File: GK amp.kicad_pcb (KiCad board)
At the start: 2 copper layers, 205.7 x 137.2 mm, 84 parts, among them J1 SPEAKER, J2 SPEAKER, J3 Direct Out, J4 AudioJack3, J5 IN, Q1 MPSA06, Q10 MJ-15002, Q11 TIP31, Q12 MPSA06, Q13 MPSA56*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

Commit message: Fix up footprints and layout PCB
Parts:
- C1, C3: footprint Capacitors_THT:C_Disc_D3.0mm_W1.6mm_P2.50mm -> Capacitor_THT:C_Rect_L9.0mm_W3.3mm_P7.50mm_MKT
- C10, C11: footprint Capacitors_THT:CP_Axial_L38.0mm_D18.0mm_P44.00mm_Horizontal -> Capacitor_THT:C_Rect_L9.0mm_W3.3mm_P7.50mm_MKT
- C12, C13, C14, C15: footprint Capacitors_THT:CP_Axial_L38.0mm_D18.0mm_P44.00mm_Horizontal -> Capacitor_THT:CP_Axial_L30.0mm_D18.0mm_P35.00mm_Horizontal
- C16, C17: footprint Capacitors_THT:CP_Axial_L38.0mm_D18.0mm_P44.00mm_Horizontal -> Capacitor_THT:CP_Axial_L10.0mm_D6.0mm_P15.00mm_Horizontal
- C18, C19: footprint Capacitors_THT:C_Disc_D3.0mm_W2.0mm_P2.50mm -> Capacitor_THT:C_Rect_L9.0mm_W3.3mm_P7.50mm_MKT
- C2: footprint Capacitors_THT:C_Axial_L3.8mm_D2.6mm_P7.50mm_Horizontal -> Capacitor_THT:CP_Radial_D8.0mm_P5.00mm
- C4, C5, C6: footprint Capacitors_THT:C_Disc_D11.0mm_W5.0mm_P5.00mm -> Capacitor_THT:C_Rect_L9.0mm_W3.3mm_P7.50mm_MKT
- C7: footprint Capacitors_THT:C_Axial_L3.8mm_D2.6mm_P7.50mm_Horizontal -> Capacitor_THT:C_Rect_L9.0mm_W3.3mm_P7.50mm_MKT
- J1, J2, J3, J5: footprint Connector_PinHeader_2.00mm:PinHeader_1x03_P2.00mm_Vertical -> Connector_Audio:Jack_3.5mm_CUI_SJ1-3533NG_Horizontal
- Q1, Q12, Q3, Q5: footprint Package_TO_SOT_THT:TO-92_Inline -> Package_TO_SOT_THT:TO-92_Inline_Wide
- Q2, Q9: footprint MJE15030:TO254P1042X498X2993-3 -> Package_TO_SOT_THT:TO-220-3_Vertical
- Q7: footprint MJE15031:TO254P1042X498X2993-3 -> Package_TO_SOT_THT:TO-220-3_Vertical
- R1, R10, R11, R12, R2, R3, R4, R5, R6, R7, R8, R9: footprint Resistors_THT:R_Axial_DIN0204_L3.6mm_D1.6mm_P1.90mm_Vertical -> Resistor_THT:R_Axial_DIN0207_L6.3mm_D2.5mm_P10.16mm_Horizontal
- R13: footprint Potentiometers:Potentiometer_Trimmer_Piher_PT-15v15_Horizontal_Px15.0mm_Py10.0mm_MountLS -> Potentiometer_THT:Potentiometer_Bourns_3386P_Vertical
- R14: footprint Resistors_THT:R_Axial_DIN0204_L3.6mm_D1.6mm_P2.54mm_Vertical -> Resistor_THT:R_Axial_DIN0207_L6.3mm_D2.5mm_P10.16mm_Horizontal
- R15, R16, R17, R18, R19, R20, R22, R23, R29, R30, R32, R33, R34, R35, R36, R37: footprint Resistors_THT:R_Axial_DIN0204_L3.6mm_D1.6mm_P5.08mm_Horizontal -> Resistor_THT:R_Axial_DIN0207_L6.3mm_D2.5mm_P10.16mm_Horizontal
- R21, R27: footprint Resistors_THT:R_Axial_DIN0204_L3.6mm_D1.6mm_P5.08mm_Horizontal -> Resistor_THT:R_Axial_Power_L20.0mm_W6.4mm_P22.40mm
- R24, R25, R28: footprint Resistors_THT:R_Axial_Power_L20.0mm_W6.4mm_P22.40mm -> Resistor_THT:R_Axial_Power_L20.0mm_W6.4mm_P22.40mm
- R26: footprint Resistors_THT:R_Axial_Shunt_L22.2mm_W9.5mm_PS14.30mm_P25.40mm -> Resistor_THT:R_Axial_Power_L20.0mm_W6.4mm_P22.40mm
- R31: footprint Resistors_THT:R_Axial_Power_L20.0mm_W6.4mm_P22.40mm -> Resistor_THT:R_Axial_DIN0207_L6.3mm_D2.5mm_P10.16mm_Horizontal
- T1: footprint Pin_Headers:Pin_Header_Straight_1x05_Pitch1.27mm -> Connector_PinSocket_2.54mm:PinSocket_1x05_P2.54mm_Vertical
- moved R37 150.2 mm to (54.1, 105.7)
- moved R33 149.0 mm to (64.3, 110.4), turned to 180 degrees
- moved J5 141.5 mm to (97.4, 160.3), turned to 180 degrees
- moved D8 140.8 mm to (81.2, 116.0), turned to 180 degrees
- moved C10 135.3 mm to (135.9, 140.7), turned to 180 degrees
- moved J4 130.7 mm to (128.7, 160.4), turned to 180 degrees
- moved C11 129.0 mm to (138.4, 150.1), turned to 270 degrees
- moved R1 123.2 mm to (85.1, 116.0)
- moved R36 121.2 mm to (51.4, 68.2)
- moved C6 118.9 mm to (103.6, 36.3), turned to 180 degrees
- moved Q14 115.1 mm to (78.9, 108.5), turned to 90 degrees
- moved Q1 114.3 mm to (116.8, 82.5), turned to 180 degrees
- moved Q12 111.4 mm to (69.8, 68.5), turned to 270 degrees
- moved R3 108.5 mm to (108.6, 98.4), turned to 90 degrees
- moved Q13 108.3 mm to (69.5, 108.7), turned to 270 degrees
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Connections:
- R1 pad 2: Net-(J5-Pad1) -> Net-(J5-PadT)
- R2 pad 1: Net-(J5-Pad1) -> Net-(J5-PadT)
- R27 pad 2: Net-(J1-Pad1) -> Net-(J1-PadT)
- R29 pad 2: Net-(J3-Pad1) -> Net-(J3-PadT)
- R30 pad 1: Net-(J3-Pad1) -> Net-(J3-PadT)
- T1 pad 1: (no net) -> Net-(T1-Pad1)
- T1 pad 2: (no net) -> Net-(T1-Pad2)
- U1 pad 1: (no net) -> Net-(U1-Pad1)
- U1 pad 5: (no net) -> Net-(U1-Pad5)
- U1 pad 8: (no net) -> Net-(U1-Pad8)
- U2 pad 1: A -> D
- U2 pad 2: Net-(T1-Pad3) -> Net-(T1-Pad5)
- U2 pad 3: D -> Net-(T1-Pad3)
- U2 pad 4: Net-(T1-Pad5) -> A
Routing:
- net Net-(C7-Pad1): track 0.00 -> 328.3 mm
- net Net-(C3-Pad1): track 0.00 -> 179.5 mm
- net Net-(C5-Pad1): track 0.00 -> 114.0 mm
- net Net-(Q8-Pad3): track 0.00 -> 84.1 mm
- net Net-(Q10-Pad3): track 0.00 -> 69.9 mm
- net Net-(J3-PadT): track 0.00 -> 64.2 mm
- net Net-(C2-Pad1): track 0.00 -> 56.6 mm
- net Net-(D2-Pad2): track 0.00 -> 48.7 mm
- net Net-(J5-PadT): track 0.00 -> 47.7 mm
- net Net-(C19-Pad1): track 0.00 -> 47.1 mm
- net Net-(C1-Pad2): track 0.00 -> 46.7 mm
- net Net-(Q10-Pad1): track 0.00 -> 46.4 mm
- net Net-(D1-Pad2): track 0.00 -> 45.1 mm
- net Net-(R29-Pad1): track 0.00 -> 44.5 mm
- net Net-(Q7-Pad3): track 0.00 -> 42.8 mm
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- added copper zone on F.Cu, net D

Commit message: rearange the board a little
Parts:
- C1: value .1 -> .1uf
- C10, C11: value 1F -> 1uf
- C12, C13, C14, C15: value 500 -> 500uf
- C16, C17, C2: value 10 -> 10uf
- C5: value .01 -> .01uf
- C6: value .1F -> .1uf
- C7: value 220 -> 220uf
- D4, D5, D6: footprint Diode_THT:D_DO-41_SOD81_P7.62mm_Horizontal -> Diode_THT:D_DO-41_SOD81_P10.16mm_Horizontal
- D7, D8: footprint Diode_THT:D_DO-41_SOD81_P10.16mm_Horizontal -> Diode_THT:D_DO-35_SOD27_P7.62mm_Horizontal
- R28: value 5 5W -> 5 5w
- moved C6 84.4 mm to (188.0, 39.4), turned to 90 degrees
- moved R28 77.4 mm to (195.6, 54.6), turned to 90 degrees
- moved R1 44.7 mm to (121.3, 142.2), turned to 180 degrees
- moved J5 26.4 mm to (123.8, 160.7)
- moved R2 24.9 mm to (121.3, 133.3), turned to 90 degrees
- moved C2 15.7 mm to (116.8, 109.4)
- moved D1 14.2 mm to (133.3, 114.2)
- moved R4 13.3 mm to (125.7, 113.7)
- moved J4 12.2 mm to (141.0, 160.7)
- moved C10 11.7 mm to (147.3, 138.2)
- moved C11 11.7 mm to (149.9, 147.6)
- moved R37 10.0 mm to (64.1, 105.4), turned to 180 degrees
- moved J3 7.75 mm to (179.0, 26.6)
- moved R31 6.81 mm to (139.7, 118.7)
- moved U2 5.88 mm to (62.1, 98.5)
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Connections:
- T1 pad 1: Net-(T1-Pad1) -> (no net)
- T1 pad 2: Net-(T1-Pad2) -> (no net)
- U1 pad 1: Net-(U1-Pad1) -> (no net)
- U1 pad 5: Net-(U1-Pad5) -> (no net)
- U1 pad 8: Net-(U1-Pad8) -> (no net)
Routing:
- net Net-(J5-PadT): track 47.7 -> 34.6 mm
- net Net-(C2-Pad1): track 56.6 -> 45.2 mm
- net Net-(C1-Pad2): track 46.7 -> 57.5 mm
- net C: track 35.9 -> 45.2 mm
- net Net-(J3-PadT): track 64.2 -> 55.1 mm
- net Net-(T1-Pad5): track 17.6 -> 26.2 mm
- net Net-(Q1-Pad3): track 19.0 -> 27.5 mm
- net Net-(C6-Pad2): track 13.5 -> 7.76 mm
- net Net-(C1-Pad1): track 11.2 -> 5.87 mm
- net Net-(C7-Pad1): track 328.3 -> 332.7 mm
- net Net-(T1-Pad3): track 21.9 -> 26.0 mm
- net GND: track 3.94 -> 0.00 mm
- net Net-(C10-Pad2): track 33.4 -> 29.8 mm
- net Net-(C19-Pad2): track 16.9 -> 20.2 mm
- net Net-(Q14-Pad3): track 30.4 -> 27.7 mm
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
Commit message: leave room for heatsink
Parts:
- moved Q9 32.5 mm to (194.3, 117.5)
- moved C7 23.3 mm to (182.9, 142.2)
- moved R24 19.1 mm to (202.6, 116.8)
- moved D4 17.7 mm to (186.7, 148.0), turned to 0 degrees
- moved R18 8.81 mm to (188.0, 142.9)
- moved Q10 7.44 mm to (225.7, 141.6)
- moved R17 1.31 mm to (186.1, 126.4), turned to 0 degrees
- turned R35 to 90 degrees
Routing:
- net D: track 32.6 -> 0.00 mm
- net Net-(Q10-Pad1): track 46.4 -> 63.2 mm
- net Net-(C5-Pad1): track 114.0 -> 97.6 mm
- net Net-(C7-Pad2): track 19.5 -> 13.1 mm
- net Net-(Q10-Pad3): track 69.9 -> 68.8 mm
- net Net-(C7-Pad1): track 332.7 -> 331.8 mm

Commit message: more layout changes
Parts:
- moved J3 136.0 mm to (152.4, 160.0), turned to 180 degrees
- moved R30 104.4 mm to (157.5, 142.2)
- moved R29 49.9 mm to (147.3, 132.1), turned to 270 degrees
- moved R7 47.1 mm to (160.7, 90.2), turned to 180 degrees
- moved C4 41.7 mm to (165.1, 73.5), turned to 180 degrees
- moved R28 39.4 mm to (156.5, 50.0)
- moved D2 38.3 mm to (172.7, 83.8), turned to 0 degrees
- moved Q7 38.1 mm to (189.5, 64.8), turned to 0 degrees
- moved D3 35.3 mm to (177.8, 27.9)
- moved R16 32.9 mm to (185.4, 40.6)
- moved R22 28.6 mm to (172.5, 76.2)
- moved Q4 26.0 mm to (162.4, 101.3), turned to 0 degrees
- moved D5 25.8 mm to (195.6, 48.3), turned to 90 degrees
- moved Q5 23.9 mm to (195.6, 27.9), turned to 270 degrees
- moved R12 23.8 mm to (189.5, 91.6), turned to 90 degrees
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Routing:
- net Net-(D2-Pad2): track 48.7 -> 14.0 mm
- net Net-(C7-Pad1): track 331.8 -> 299.5 mm
- net Net-(C5-Pad1): track 97.6 -> 65.6 mm
- net Net-(Q10-Pad1): track 63.2 -> 94.5 mm
- net Net-(J3-PadT): track 55.1 -> 27.1 mm
- net Net-(R12-Pad1): track 7.62 -> 28.3 mm
- net Net-(Q1-Pad2): track 21.9 -> 41.1 mm
- net Net-(Q7-Pad3): track 42.8 -> 60.0 mm
- net Net-(Q8-Pad3): track 84.1 -> 69.5 mm
- net Net-(R26-Pad2): track 26.8 -> 12.7 mm
- net Net-(C10-Pad2): track 29.8 -> 43.3 mm
- net Net-(D2-Pad1): track 36.0 -> 48.8 mm
- net Net-(D3-Pad1): track 30.3 -> 17.8 mm
- net Net-(C1-Pad2): track 57.5 -> 46.0 mm
- net Net-(Q1-Pad3): track 27.5 -> 16.3 mm
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
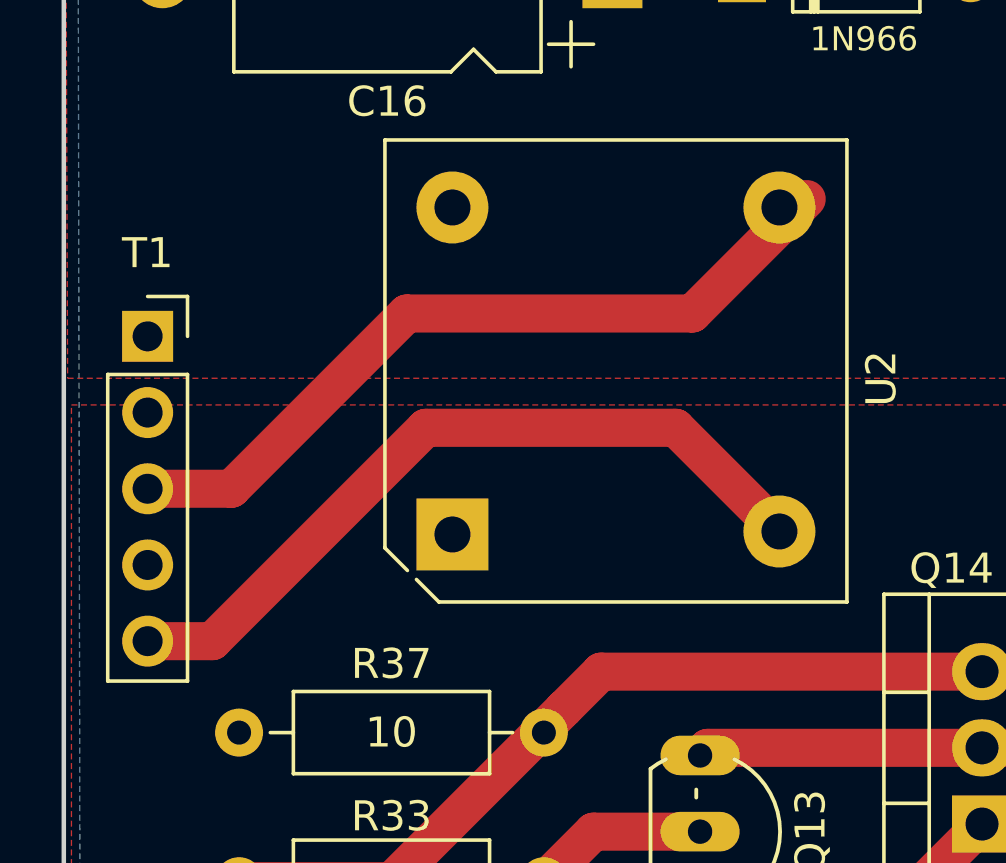
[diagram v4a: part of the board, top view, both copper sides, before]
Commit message: fix power input
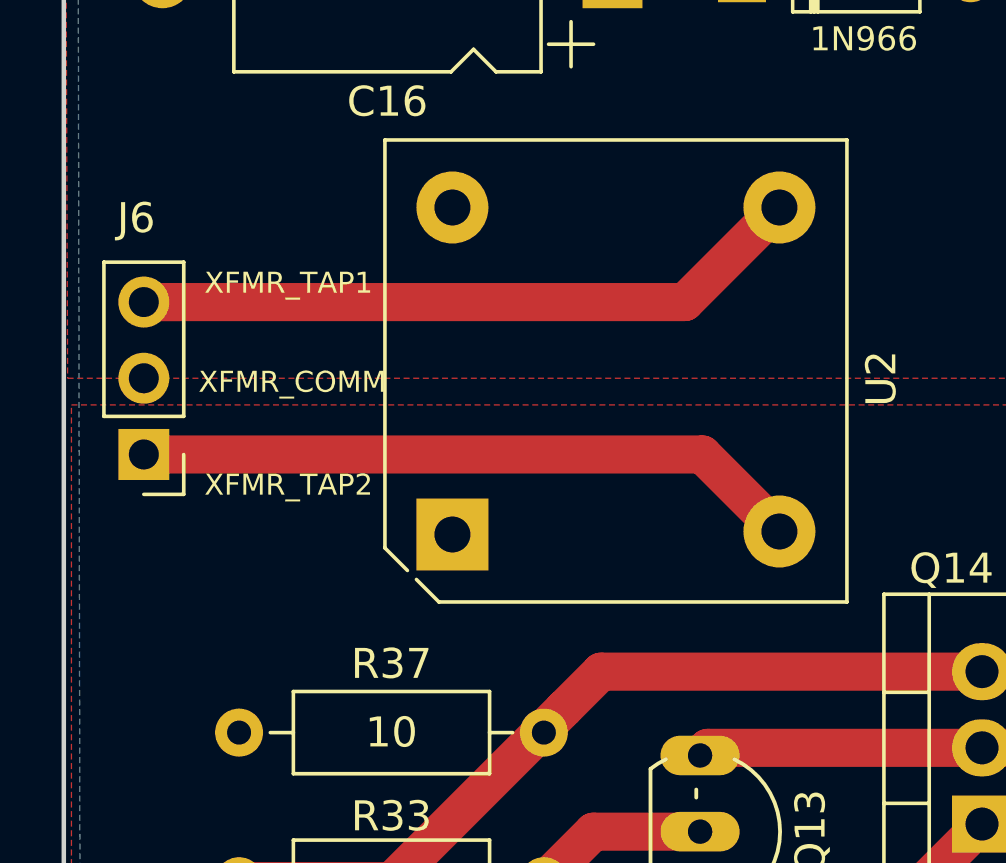
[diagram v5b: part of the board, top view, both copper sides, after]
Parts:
- removed T1: Xformer, Connector_PinSocket_2.54mm:PinSocket_1x05_P2.54mm_Vertical
- added J6: Conn_01x03_Male, Connector_PinHeader_2.54mm:PinHeader_1x03_P2.54mm_Vertical, F.Cu at (50.9, 96.1)
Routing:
- net Net-(J6-Pad1): track 25.4 -> 22.3 mm
- net Net-(J6-Pad3): track 26.0 -> 23.7 mm
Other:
- board text added: "XFMR_COMM"
- board text added: "XFMR_TAP1"
- board text added: "XFMR_TAP2"
